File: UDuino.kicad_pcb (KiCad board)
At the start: 2 copper layers, 127 parts, among them J1 Screw_Terminal_01x04, J2 PMOD1, J3 Conn_01x04_Male, J4 Conn_01x04_Male, J5 Conn_01x03_Male, J6 Conn_01x03_Male, Q1 TRANS_PNP-MMBT4403, Q2 TRANS_PNP-MMBT4403, Q3 TRANS_PNP-MMBT4403, Q4 TRANS_PNP-MMBT4403, U1 NAU8315YG, U2 DRV8833RTY, U3 NAU8315YG, U4 STM32L452VCTx, U5 LTC3111EDE, U6 LTC3111EDE

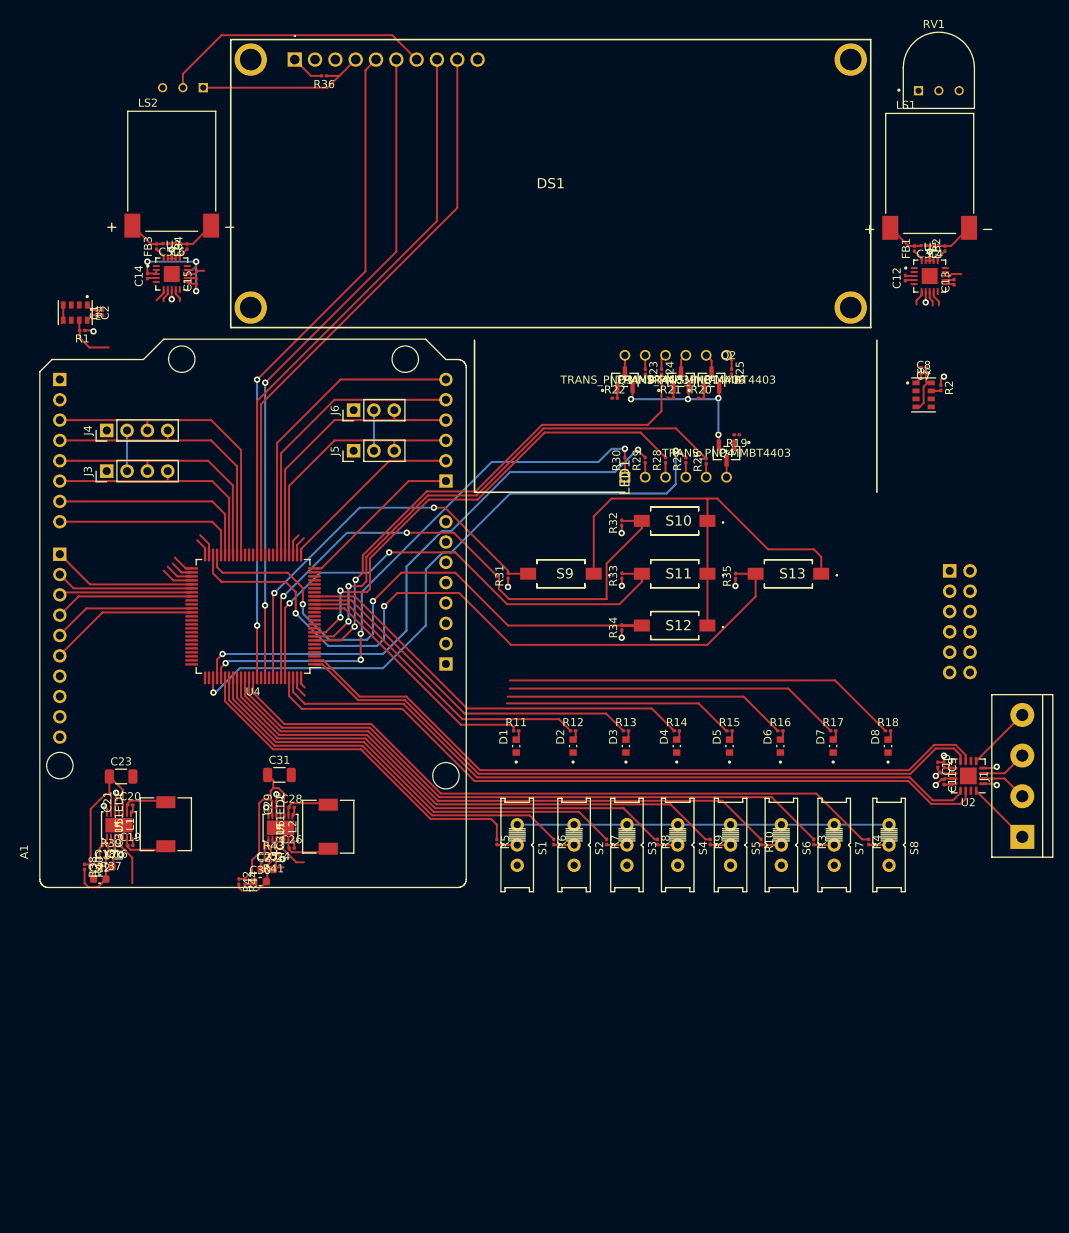
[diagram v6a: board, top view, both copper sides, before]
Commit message: First week after winter break. Changed Power circuit design to use different DC to DC converter Setting correct footprints for the components like resistors and capacitors.
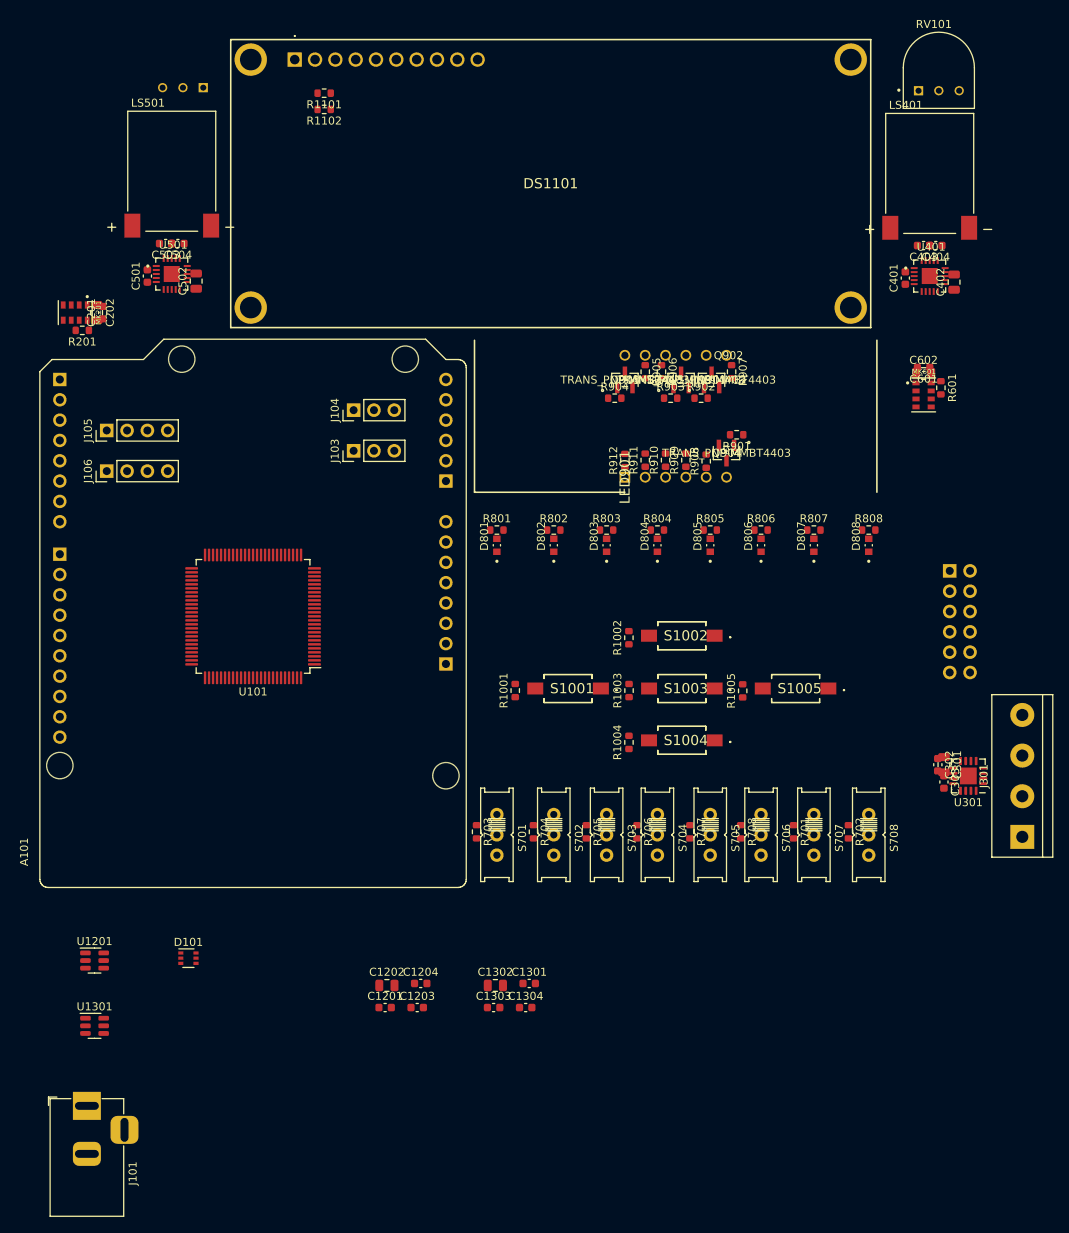
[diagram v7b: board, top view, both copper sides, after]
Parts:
- removed C16, C18, C24, C25: 27pF, Capacitor_SMD:C_0201_0603Metric
- removed C17, C27: 680pF, Capacitor_SMD:C_0603_1608Metric
- removed C19, C20, C26, C28: 0u1, Capacitor_SMD:C_0201_0603Metric
- removed C21, C29: 1µF, Capacitor_SMD:C_0201_0603Metric
- removed C22, C30: 33pF, Capacitor_SMD:C_0603_1608Metric
- removed C23, C31: 22µF, Capacitor_SMD:C_1206_3216Metric
- removed FB1, FB2, FB3, FB4: FerriteBead, Inductor_SMD:L_0201_0603Metric
- removed L1, L2: 4u7, Inductor_SMD:L_6.3x6.3_H3
- removed R37, R41: 26.1k, Resistor_SMD:R_0201_0603Metric
- removed R38, R42: 1M, Resistor_SMD:R_0201_0603Metric
- removed R39: 191k, Resistor_SMD:R_0201_0603Metric
- removed R40, R44: 20k, Resistor_SMD:R_0201_0603Metric
- removed R43: 320k, Resistor_SMD:R_0201_0603Metric
- removed U5, U6: LTC3111EDE, Custom:LTC3111EDE-TRPBF
- added C1201: 10u, Capacitor_SMD:C_0603_1608Metric, F.Cu at (72.4, 171.2)
- added C1202: 100n, Capacitor_SMD:C_0805_2012Metric, F.Cu at (72.6, 168.4)
- added C1203: 22u, Capacitor_SMD:C_0603_1608Metric, F.Cu at (76.4, 171.2)
- added C1204: 22u, Capacitor_SMD:C_0603_1608Metric, F.Cu at (76.8, 168.2)
- added C1301: 10u, Capacitor_SMD:C_0603_1608Metric, F.Cu at (90.4, 168.2)
- added C1302: 100n, Capacitor_SMD:C_0805_2012Metric, F.Cu at (86.2, 168.4)
- added C1303: 22u, Capacitor_SMD:C_0603_1608Metric, F.Cu at (86.0, 171.2)
- added C1304: 22u, Capacitor_SMD:C_0603_1608Metric, F.Cu at (90.0, 171.2)
- added D101: BAS70TW, Package_TO_SOT_SMD:SOT-363_SC-70-6, F.Cu at (47.8, 165.0)
- added J101: Barrel_Jack, Connector_BarrelJack:BarrelJack_Horizontal, F.Cu at (35.1, 183.5)
- added R1102: 100, Resistor_SMD:R_0603_1608Metric, F.Cu at (64.8, 58.9)
- added U1201: AP63205WU, Package_TO_SOT_SMD:TSOT-23-6, F.Cu at (36.1, 165.3)
- added U1301: AP63203WU, Package_TO_SOT_SMD:TSOT-23-6, F.Cu at (36.1, 173.5)
- C201: renamed from C1; footprint Capacitor_SMD:C_0201_0603Metric -> Capacitor_SMD:C_0603_1608Metric
- C202: renamed from C2; footprint Capacitor_SMD:C_0201_0603Metric -> Capacitor_SMD:C_0805_2012Metric
- C301: renamed from C9; footprint Capacitor_SMD:C_0201_0603Metric -> Capacitor_SMD:C_0805_2012Metric
- C302: renamed from C10; footprint Capacitor_SMD:C_0201_0603Metric -> Capacitor_SMD:C_0603_1608Metric
- C303: renamed from C11; footprint Capacitor_SMD:C_0201_0603Metric -> Capacitor_SMD:C_0603_1608Metric
- C401: renamed from C12; footprint Capacitor_SMD:C_0201_0603Metric -> Capacitor_SMD:C_0603_1608Metric
- C402: renamed from C13; value 0u1 -> 100n; footprint Capacitor_SMD:C_0201_0603Metric -> Capacitor_SMD:C_0805_2012Metric
- C403: renamed from C3; footprint Capacitor_SMD:C_0201_0603Metric -> Capacitor_SMD:C_0603_1608Metric
- C404: renamed from C4; footprint Capacitor_SMD:C_0201_0603Metric -> Capacitor_SMD:C_0603_1608Metric
- C501: renamed from C14; footprint Capacitor_SMD:C_0201_0603Metric -> Capacitor_SMD:C_0603_1608Metric
- C502: renamed from C15; value 0u1 -> 100n; footprint Capacitor_SMD:C_0201_0603Metric -> Capacitor_SMD:C_0805_2012Metric
- C503: renamed from C5; footprint Capacitor_SMD:C_0201_0603Metric -> Capacitor_SMD:C_0603_1608Metric
- C504: renamed from C6; footprint Capacitor_SMD:C_0201_0603Metric -> Capacitor_SMD:C_0603_1608Metric
- C601: renamed from C7; footprint Capacitor_SMD:C_0201_0603Metric -> Capacitor_SMD:C_0603_1608Metric
- C602: renamed from C8; footprint Capacitor_SMD:C_0201_0603Metric -> Capacitor_SMD:C_0805_2012Metric
- R1001: renamed from R31; footprint Resistor_SMD:R_0201_0603Metric -> Resistor_SMD:R_0603_1608Metric
- R1002: renamed from R32; footprint Resistor_SMD:R_0201_0603Metric -> Resistor_SMD:R_0603_1608Metric
- R1003: renamed from R33; footprint Resistor_SMD:R_0201_0603Metric -> Resistor_SMD:R_0603_1608Metric
- R1004: renamed from R34; footprint Resistor_SMD:R_0201_0603Metric -> Resistor_SMD:R_0603_1608Metric
- R1005: renamed from R35; footprint Resistor_SMD:R_0201_0603Metric -> Resistor_SMD:R_0603_1608Metric
- R1101: renamed from R36; value 50 -> 100; footprint Resistor_SMD:R_0201_0603Metric -> Resistor_SMD:R_0603_1608Metric
- R201: renamed from R1; footprint Resistor_SMD:R_0201_0603Metric -> Resistor_SMD:R_0603_1608Metric
- R601: renamed from R2; footprint Resistor_SMD:R_0201_0603Metric -> Resistor_SMD:R_0603_1608Metric
- R701: renamed from R3; footprint Resistor_SMD:R_0201_0603Metric -> Resistor_SMD:R_0603_1608Metric
- R702: renamed from R4; footprint Resistor_SMD:R_0201_0603Metric -> Resistor_SMD:R_0603_1608Metric
- R703: renamed from R5; footprint Resistor_SMD:R_0201_0603Metric -> Resistor_SMD:R_0603_1608Metric
- R704: renamed from R6; footprint Resistor_SMD:R_0201_0603Metric -> Resistor_SMD:R_0603_1608Metric
- R705: renamed from R7; footprint Resistor_SMD:R_0201_0603Metric -> Resistor_SMD:R_0603_1608Metric
- R706: renamed from R8; footprint Resistor_SMD:R_0201_0603Metric -> Resistor_SMD:R_0603_1608Metric
- R707: renamed from R9; footprint Resistor_SMD:R_0201_0603Metric -> Resistor_SMD:R_0603_1608Metric
- R708: renamed from R10; footprint Resistor_SMD:R_0201_0603Metric -> Resistor_SMD:R_0603_1608Metric
- R801: renamed from R11; footprint Resistor_SMD:R_0201_0603Metric -> Resistor_SMD:R_0603_1608Metric
- R802: renamed from R12; footprint Resistor_SMD:R_0201_0603Metric -> Resistor_SMD:R_0603_1608Metric
- R803: renamed from R13; footprint Resistor_SMD:R_0201_0603Metric -> Resistor_SMD:R_0603_1608Metric
- R804: renamed from R14; footprint Resistor_SMD:R_0201_0603Metric -> Resistor_SMD:R_0603_1608Metric
- R805: renamed from R15; footprint Resistor_SMD:R_0201_0603Metric -> Resistor_SMD:R_0603_1608Metric
- R806: renamed from R16; footprint Resistor_SMD:R_0201_0603Metric -> Resistor_SMD:R_0603_1608Metric
- R807: renamed from R17; footprint Resistor_SMD:R_0201_0603Metric -> Resistor_SMD:R_0603_1608Metric
- R808: renamed from R18; footprint Resistor_SMD:R_0201_0603Metric -> Resistor_SMD:R_0603_1608Metric
- R901: renamed from R19; footprint Resistor_SMD:R_0201_0603Metric -> Resistor_SMD:R_0603_1608Metric
- R902: renamed from R20; footprint Resistor_SMD:R_0201_0603Metric -> Resistor_SMD:R_0603_1608Metric
- R903: renamed from R21; footprint Resistor_SMD:R_0201_0603Metric -> Resistor_SMD:R_0603_1608Metric
- R904: renamed from R22; footprint Resistor_SMD:R_0201_0603Metric -> Resistor_SMD:R_0603_1608Metric
- R905: renamed from R23; footprint Resistor_SMD:R_0201_0603Metric -> Resistor_SMD:R_0603_1608Metric
- R906: renamed from R24; footprint Resistor_SMD:R_0201_0603Metric -> Resistor_SMD:R_0603_1608Metric
- R907: renamed from R25; footprint Resistor_SMD:R_0201_0603Metric -> Resistor_SMD:R_0603_1608Metric
- R908: renamed from R26; footprint Resistor_SMD:R_0201_0603Metric -> Resistor_SMD:R_0603_1608Metric
- R909: renamed from R27; footprint Resistor_SMD:R_0201_0603Metric -> Resistor_SMD:R_0603_1608Metric
- R910: renamed from R28; footprint Resistor_SMD:R_0201_0603Metric -> Resistor_SMD:R_0603_1608Metric
- R911: renamed from R29; footprint Resistor_SMD:R_0201_0603Metric -> Resistor_SMD:R_0603_1608Metric
- R912: renamed from R30; footprint Resistor_SMD:R_0201_0603Metric -> Resistor_SMD:R_0603_1608Metric
- RV101: renamed from RV1; value R_Potentiometer -> 100k
- moved R802 25.2 mm to (93.5, 111.5)
- moved R803 25.2 mm to (100.1, 111.5)
- moved R806 25.2 mm to (119.4, 111.5)
- moved R801 25.2 mm to (86.4, 111.5)
- moved R804 25.2 mm to (106.4, 111.5)
- moved R805 25.2 mm to (113.0, 111.5)
- moved R807 25.2 mm to (126.0, 111.5)
- moved R808 25.2 mm to (132.8, 111.5)
- moved D802 25.2 mm to (93.5, 113.4)
- moved D803 25.2 mm to (100.1, 113.4)
- moved D806 25.2 mm to (119.4, 113.4)
- moved D801 25.2 mm to (86.4, 113.4)
- moved D804 25.2 mm to (106.4, 113.4)
- moved D805 25.2 mm to (113.0, 113.4)
- moved D807 25.2 mm to (126.0, 113.4)
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- renumbered A1 to A101, D1 to D801, D2 to D802, D3 to D803, D4 to D804, D5 to D805, D6 to D806, D7 to D807, D8 to D808, DS1 to DS1101, J2 to J102, J5 to J103, J6 to J104, J4 to J105, J3 to J106, J1 to J301, LED1 to LED901, LS1 to LS401, LS2 to LS501, MK1 to MK201, MK2 to MK601, Q1 to Q901, Q2 to Q902, Q3 to Q903, Q4 to Q904, RV2 to RV1101, S9 to S1001, S10 to S1002, S11 to S1003, S12 to S1004, S13 to S1005, S1 to S701, S2 to S702, S3 to S703, S4 to S704, S5 to S705, S6 to S706, S7 to S707, S8 to S708, U4 to U101, U2 to U301, U1 to U401, U3 to U501
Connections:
- net Net-(A1-PadD10) renamed /D10
- net Net-(A1-PadD11) renamed /D11
- net Net-(A1-PadD12) renamed /D12
- net Net-(A1-PadD13) renamed /D13
- net Net-(A1-PadD8) renamed /D8
- net Net-(A1-PadD9) renamed /D9
- A101 pad D3: /D4 -> /D3
- A101 pad VIN: unconnected-(A1-PadVIN) -> /V_IN
- C403 pad 2: Net-(C3-Pad2) -> Net-(C403-Pad2)
- C404 pad 1: Net-(C4-Pad1) -> Net-(C404-Pad1)
- C503 pad 2: Net-(C5-Pad2) -> Net-(C503-Pad2)
- C504 pad 1: Net-(C6-Pad1) -> Net-(C504-Pad1)
- J105 pad 4: /D4 -> /D3
- LS401 pad N: Net-(C4-Pad1) -> Net-(C404-Pad1)
- LS401 pad P: Net-(C3-Pad2) -> Net-(C403-Pad2)
- LS501 pad N: Net-(C6-Pad1) -> Net-(C504-Pad1)
- LS501 pad P: Net-(C5-Pad2) -> Net-(C503-Pad2)
- U101 pad 42: /D4 -> /D3
- U401 pad 16: Net-(FB2-Pad1) -> Net-(C404-Pad1)
- U401 pad 20: Net-(FB1-Pad1) -> Net-(C403-Pad2)
- U501 pad 16: Net-(FB4-Pad1) -> Net-(C504-Pad1)
- U501 pad 20: Net-(FB3-Pad1) -> Net-(C503-Pad2)
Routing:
- net +3V3: track 173.0 -> 0.00 mm, vias 3 -> 0
- net /Motor/AIN1: track 93.7 -> 0.00 mm
- net /Motor/AIN2: track 91.5 -> 0.00 mm
- net /Buttons/BT5: track 91.1 -> 0.00 mm, vias 2 -> 0
- net /Motor/BIN1: track 89.7 -> 0.00 mm
- net /Motor/BIN2: track 88.8 -> 0.00 mm
- net /SW8: track 86.4 -> 0.00 mm
- net /SPI3_MOSI: track 84.1 -> 0.00 mm, vias 2 -> 0
- net /SPI3_SCK: track 83.4 -> 0.00 mm, vias 2 -> 0
- net /7Seg/C: track 80.4 -> 0.00 mm, vias 2 -> 0
- net /SW7: track 80.2 -> 0.00 mm
- net /SW6: track 74.2 -> 0.00 mm
- net /Buttons/BT2: track 72.4 -> 0.00 mm, vias 2 -> 0
- net /LCD/RS: track 72.1 -> 0.00 mm
- net /7Seg/D: track 71.8 -> 0.00 mm, vias 2 -> 0
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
